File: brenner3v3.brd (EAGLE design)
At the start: 100 x 80 mm, 14 parts, among them IC1 REG1117, Q2 BC328, Q3 BC328

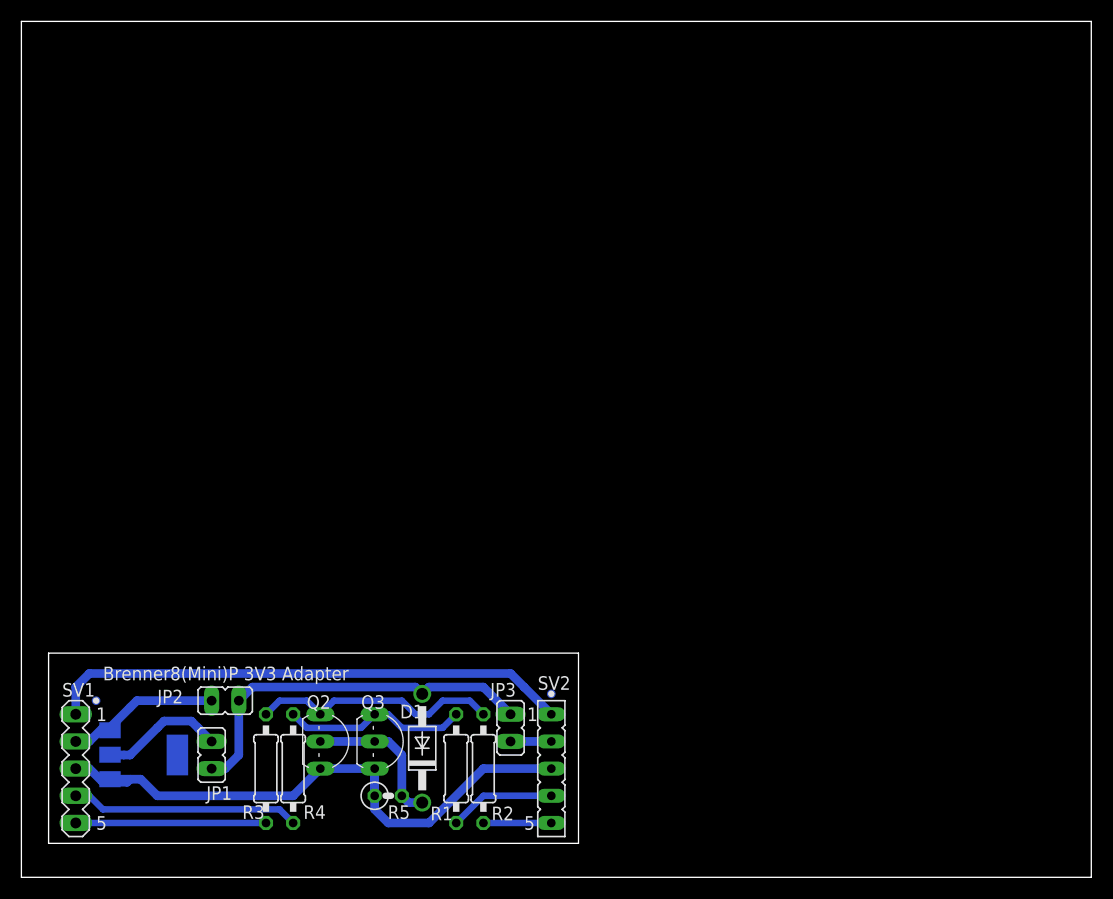
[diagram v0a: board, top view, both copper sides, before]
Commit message: Removed outer dimensions
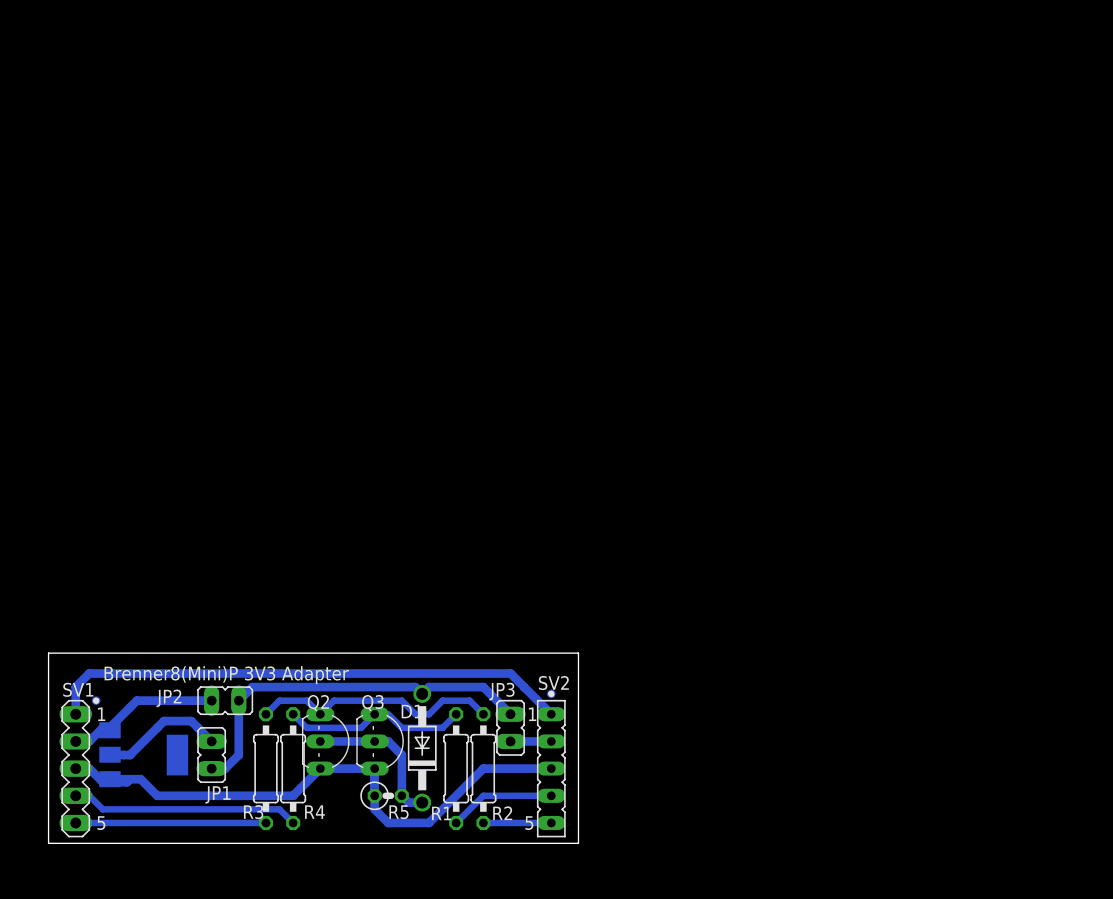
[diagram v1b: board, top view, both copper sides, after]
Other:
- board size 100 x 80 mm -> 49.5 x 17.8 mm
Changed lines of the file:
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@@
 <board>
 <plain>
-<wire x1="0" y1="0" x2="100" y2="0" width="0" layer="20"/>
-<wire x1="100" y1="0" x2="100" y2="80" width="0" layer="20"/>
-<wire x1="100" y1="80" x2="0" y2="80" width="0" layer="20"/>
-<wire x1="0" y1="80" x2="0" y2="0" width="0" layer="20"/>
 <wire x1="2.54" y1="3.175" x2="52.07" y2="3.175" width="0" layer="20"/>
 <wire x1="52.07" y1="3.175" x2="52.07" y2="20.955" width="0" layer="20"/>
